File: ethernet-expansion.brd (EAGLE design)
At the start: 64.4 x 44.4 mm, 22 parts, among them Q1 25MHz, U1 ENC28J60-SO

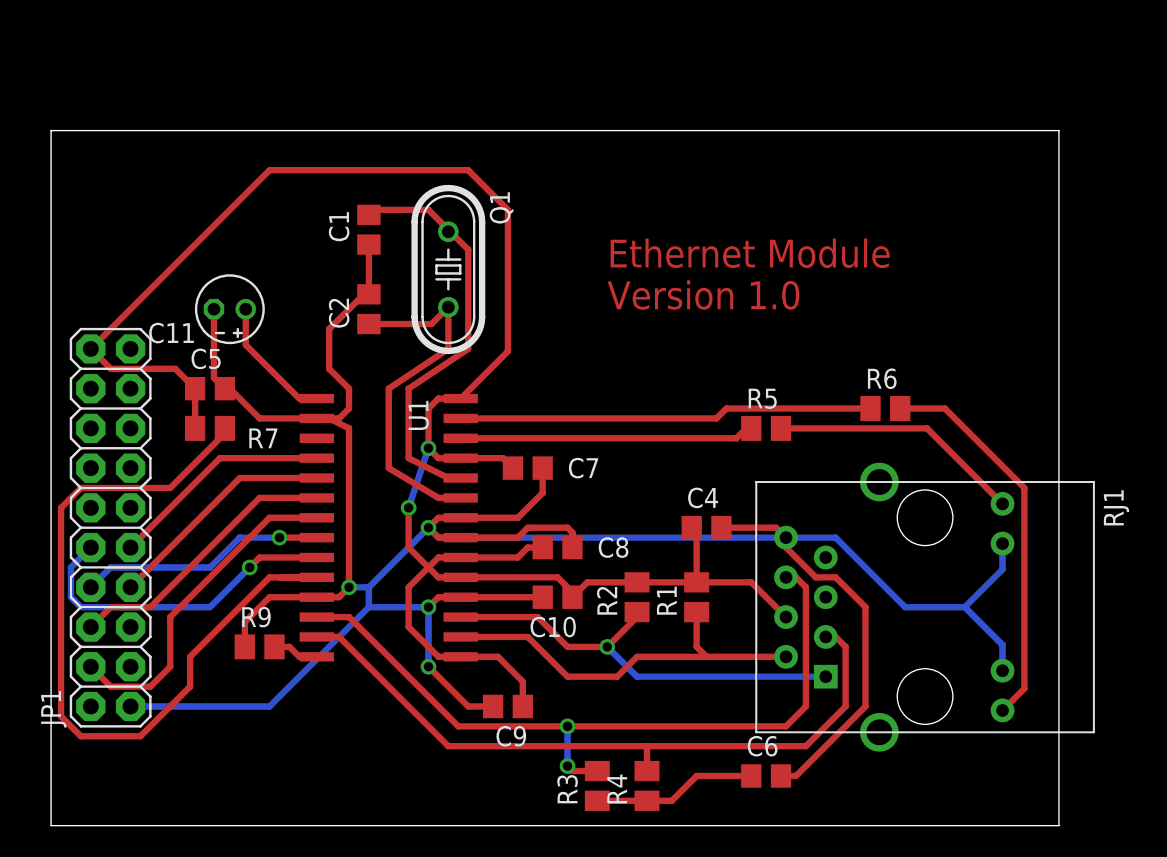
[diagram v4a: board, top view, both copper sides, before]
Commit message: Rotated oscillator to get a better Vdd trace
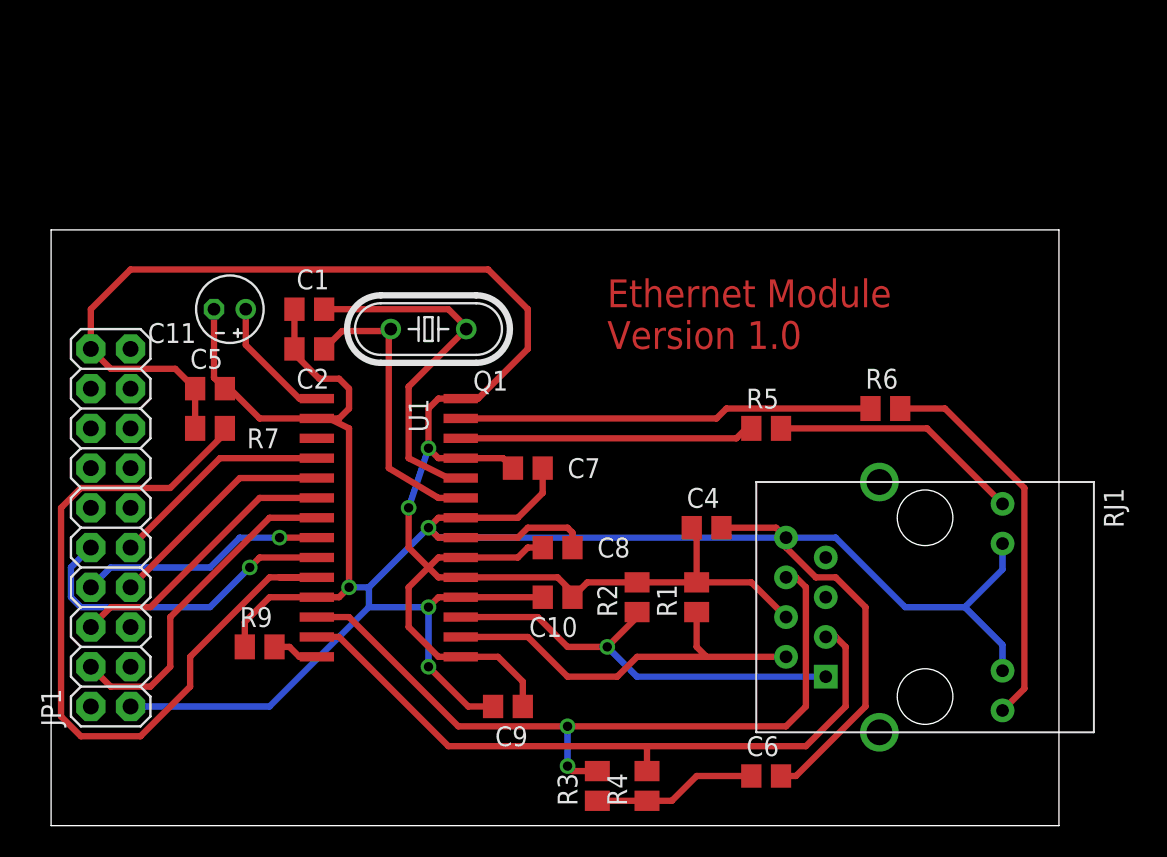
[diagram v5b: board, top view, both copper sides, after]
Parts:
- moved C1 6.35 mm to (16.5, 33.0), turned to 180 degrees
- moved C2 4.58 mm to (16.5, 30.5), turned to 180 degrees
- moved Q1 4.02 mm to (24.1, 31.8), turned to 180 degrees
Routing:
- net +3V3: track 126.5 -> 121.4 mm
- net N$12: track 23.0 -> 18.7 mm
- net GND: track 186.0 -> 182.2 mm
- net N$11: track 26.6 -> 23.1 mm
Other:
- board size 64.4 x 44.4 mm -> 64.4 x 38.1 mm
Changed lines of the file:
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@@
 <plain>
 <wire x1="0" y1="0" x2="64.44" y2="0" width="0" layer="20"/>
-<wire x1="64.44" y1="0" x2="64.44" y2="44.44" width="0" layer="20"/>
-<wire x1="64.44" y1="44.44" x2="0" y2="44.44" width="0" layer="20"/>
-<wire x1="0" y1="44.44" x2="0" y2="0" width="0" layer="20"/>
-<text x="35.56" y="33.02" size="1.778" layer="1">Ethernet Module
+<wire x1="64.44" y1="0" x2="64.44" y2="38.09" width="0" layer="20"/>
+<wire x1="64.44" y1="38.09" x2="0" y2="38.09" width="0" layer="20"/>
+<wire x1="0" y1="38.09" x2="0" y2="0" width="0" layer="20"/>
+<text x="35.56" y="30.48" size="1.778" layer="1">Ethernet Module
 Version 1.0</text>
 </plain>
@@
 <attribute name="NAME" x="44.45" y="4.445" size="1.27" layer="25"/>
 </element>
-<element name="C1" library="resistor" package="C0805" value="10pF" x="20.32" y="38.1" smashed="yes" rot="R270">
-<attribute name="NAME" x="17.78" y="39.37" size="1.27" layer="25" rot="R270"/>
-</element>
-<element name="C2" library="resistor" package="C0805" value="10pF" x="20.32" y="33.02" smashed="yes" rot="R90">
-<attribute name="NAME" x="19.05" y="31.75" size="1.27" layer="25" rot="R90"/>
+<element name="C1" library="resistor" package="C0805" value="10pF" x="16.51" y="33.02" smashed="yes" rot="R180">
+<attribute name="NAME" x="17.78" y="35.56" size="1.27" layer="25" rot="R180"/>
+</element>
+<element name="C2" library="resistor" package="C0805" value="10pF" x="16.51" y="30.48" smashed="yes" rot="R180">
+<attribute name="NAME" x="17.78" y="29.21" size="1.27" layer="25" rot="R180"/>
 </element>
 <element name="C5" library="resistor" package="C0805" value="0.1uF" x="10.16" y="27.94" smashed="yes">
@@
 </element>
 <element name="JP1" library="SparkFun-Connectors" package="2X10" value="" x="3.81" y="19.05" rot="R90"/>
-<element name="Q1" library="crystal" package="HC49/S" value="25MHz" x="25.4" y="35.56" rot="R270">
-<attribute name="OC_NEWARK" value="unknown" x="25.4" y="35.56" size="1.778" layer="27" rot="R270" display="off"/>
-<attribute name="MPN" value="" x="25.4" y="35.56" size="1.778" layer="27" rot="R270" display="off"/>
-<attribute name="MF" value="" x="25.4" y="35.56" size="1.778" layer="27" rot="R270" display="off"/>
-<attribute name="OC_FARNELL" value="1667008" x="25.4" y="35.56" size="1.778" layer="27" rot="R270" display="off"/>
+<element name="Q1" library="crystal" package="HC49/S" value="25MHz" x="24.13" y="31.75" rot="R180">
+<attribute name="OC_NEWARK" value="unknown" x="24.13" y="31.75" size="1.778" layer="27" rot="R180" display="off"/>
+<attribute name="MPN" value="" x="24.13" y="31.75" size="1.778" layer="27" rot="R180" display="off"/>
+<attribute name="MF" value="" x="24.13" y="31.75" size="1.778" layer="27" rot="R180" display="off"/>
+<attribute name="OC_FARNELL" value="1667008" x="24.13" y="31.75" size="1.778" layer="27" rot="R180" display="off"/>
 </element>
 <element name="R1" library="resistor" package="M0805" value="49.9" x="41.275" y="14.605" smashed="yes" rot="R90">
@@
 <contactref element="C7" pad="1"/>
 <contactref element="RJ1" pad="P4"/>
-<wire x1="2.54" y1="30.48" x2="13.97" y2="41.91" width="0.4064" layer="1"/>
-<wire x1="13.97" y1="41.91" x2="26.67" y2="41.91" width="0.4064" layer="1"/>
-<wire x1="26.67" y1="41.91" x2="29.21" y2="39.37" width="0.4064" layer="1"/>
-<wire x1="29.21" y1="39.37" x2="29.21" y2="30.325" width="0.4064" layer="1"/>
-<wire x1="29.21" y1="30.325" x2="26.19" y2="27.305" width="0.4064" layer="1"/>
 <wire x1="2.54" y1="30.48" x2="3.81" y2="29.21" width="0.4064" layer="1"/>
 <wire x1="3.81" y1="29.21" x2="7.94" y2="29.21" width="0.4064" layer="1"/>
@@
 <wire x1="37.465" y1="15.555" x2="34.285" y2="15.555" width="0.4064" layer="1"/>
 <wire x1="34.285" y1="15.555" x2="33.335" y2="14.605" width="0.4064" layer="1"/>
+<wire x1="5.08" y1="35.56" x2="27.94" y2="35.56" width="0.4064" layer="1"/>
+<wire x1="27.94" y1="35.56" x2="30.48" y2="33.02" width="0.4064" layer="1"/>
+<wire x1="30.48" y1="33.02" x2="30.48" y2="30.48" width="0.4064" layer="1"/>
+<wire x1="30.48" y1="30.48" x2="27.305" y2="27.305" width="0.4064" layer="1"/>
+<wire x1="27.305" y1="27.305" x2="26.19" y2="27.305" width="0.4064" layer="1"/>
+<wire x1="2.54" y1="30.48" x2="2.54" y2="33.02" width="0.4064" layer="1"/>
+<wire x1="2.54" y1="33.02" x2="5.08" y2="35.56" width="0.4064" layer="1"/>
 </signal>
 <signal name="GND">
@@
 <wire x1="10.414" y1="33.02" x2="10.414" y2="28.636" width="0.4064" layer="1"/>
 <wire x1="10.414" y1="28.636" x2="11.11" y2="27.94" width="0.4064" layer="1"/>
-<wire x1="20.32" y1="37.15" x2="20.32" y2="33.97" width="0.4064" layer="1"/>
-<wire x1="20.32" y1="33.97" x2="20" y2="33.97" width="0.4064" layer="1"/>
-<wire x1="20" y1="33.97" x2="17.78" y2="31.75" width="0.4064" layer="1"/>
-<wire x1="17.78" y1="31.75" x2="17.78" y2="29.21" width="0.4064" layer="1"/>
-<wire x1="17.78" y1="29.21" x2="19.05" y2="27.94" width="0.4064" layer="1"/>
+<wire x1="15.56" y1="33.02" x2="15.56" y2="30.48" width="0.4064" layer="1"/>
+<wire x1="17.78" y1="29.21" x2="18.415" y2="28.575" width="0" layer="19" extent="1-16"/>
+<wire x1="18.415" y1="28.575" x2="19.05" y2="27.94" width="0.4064" layer="1"/>
 <wire x1="19.05" y1="27.94" x2="19.05" y2="26.67" width="0.4064" layer="1"/>
 <wire x1="19.05" y1="26.67" x2="18.415" y2="26.035" width="0.4064" layer="1"/>
@@
 <wire x1="52.07" y1="13.97" x2="52.07" y2="7.62" width="0.4064" layer="1"/>
 <wire x1="52.07" y1="7.62" x2="47.625" y2="3.175" width="0.4064" layer="1"/>
+<wire x1="15.56" y1="30.48" x2="15.56" y2="30.16" width="0.4064" layer="1"/>
+<wire x1="15.56" y1="30.16" x2="17.145" y2="28.575" width="0.4064" layer="1"/>
+<wire x1="17.145" y1="28.575" x2="18.415" y2="28.575" width="0.4064" layer="1"/>
 </signal>
 <signal name="N$8">
@@
 <contactref element="U1" pad="24"/>
 <wire x1="25.4" y1="22.225" x2="26.19" y2="22.225" width="0.4064" layer="1"/>
-<wire x1="25.4" y1="37.973" x2="25.4" y2="38.1" width="0.4064" layer="1"/>
-<wire x1="25.4" y1="38.1" x2="24.13" y2="39.37" width="0.4064" layer="1"/>
-<wire x1="24.13" y1="39.37" x2="20.64" y2="39.37" width="0.4064" layer="1"/>
-<wire x1="20.64" y1="39.37" x2="20.32" y2="39.05" width="0.4064" layer="1"/>
-<wire x1="25.4" y1="37.973" x2="25.527" y2="37.973" width="0.4064" layer="1"/>
-<wire x1="25.527" y1="37.973" x2="26.67" y2="36.83" width="0.4064" layer="1"/>
-<wire x1="26.67" y1="36.83" x2="26.67" y2="30.48" width="0.4064" layer="1"/>
-<wire x1="26.67" y1="30.48" x2="22.86" y2="27.94" width="0.4064" layer="1"/>
-<wire x1="22.86" y1="27.94" x2="22.86" y2="23.495" width="0.4064" layer="1"/>
+<wire x1="22.86" y1="28.067" x2="22.86" y2="23.495" width="0.4064" layer="1"/>
 <wire x1="22.86" y1="23.495" x2="25.4" y2="22.225" width="0.4064" layer="1"/>
+<wire x1="22.86" y1="28.067" x2="26.543" y2="31.75" width="0.4064" layer="1"/>
+<wire x1="26.543" y1="31.75" x2="26.543" y2="31.877" width="0.4064" layer="1"/>
+<wire x1="26.543" y1="31.877" x2="25.4" y2="33.02" width="0.4064" layer="1"/>
+<wire x1="25.4" y1="33.02" x2="17.46" y2="33.02" width="0.4064" layer="1"/>
 </signal>
 <signal name="N$12">
@@
 <contactref element="C2" pad="1"/>
 <contactref element="U1" pad="23"/>
-<wire x1="25.4" y1="33.147" x2="25.4" y2="30.48" width="0.4064" layer="1"/>
-<wire x1="25.4" y1="30.48" x2="21.59" y2="27.94" width="0.4064" layer="1"/>
-<wire x1="21.59" y1="27.94" x2="21.59" y2="22.86" width="0.4064" layer="1"/>
+<wire x1="21.59" y1="31.623" x2="21.59" y2="22.86" width="0.4064" layer="1"/>
 <wire x1="21.59" y1="22.86" x2="24.765" y2="20.955" width="0.4064" layer="1"/>
 <wire x1="24.765" y1="20.955" x2="26.19" y2="20.955" width="0.4064" layer="1"/>
-<wire x1="20.32" y1="32.07" x2="24.323" y2="32.07" width="0.4064" layer="1"/>
-<wire x1="24.323" y1="32.07" x2="25.4" y2="33.147" width="0.4064" layer="1"/>
+<wire x1="21.59" y1="31.623" x2="21.717" y2="31.75" width="0.4064" layer="1"/>
+<wire x1="21.59" y1="31.623" x2="18.603" y2="31.623" width="0.4064" layer="1"/>
+<wire x1="18.603" y1="31.623" x2="17.46" y2="30.48" width="0.4064" layer="1"/>
 </signal>
 <signal name="ETH_INT0">

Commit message: Adding ground fill on top layer and trying out other placements
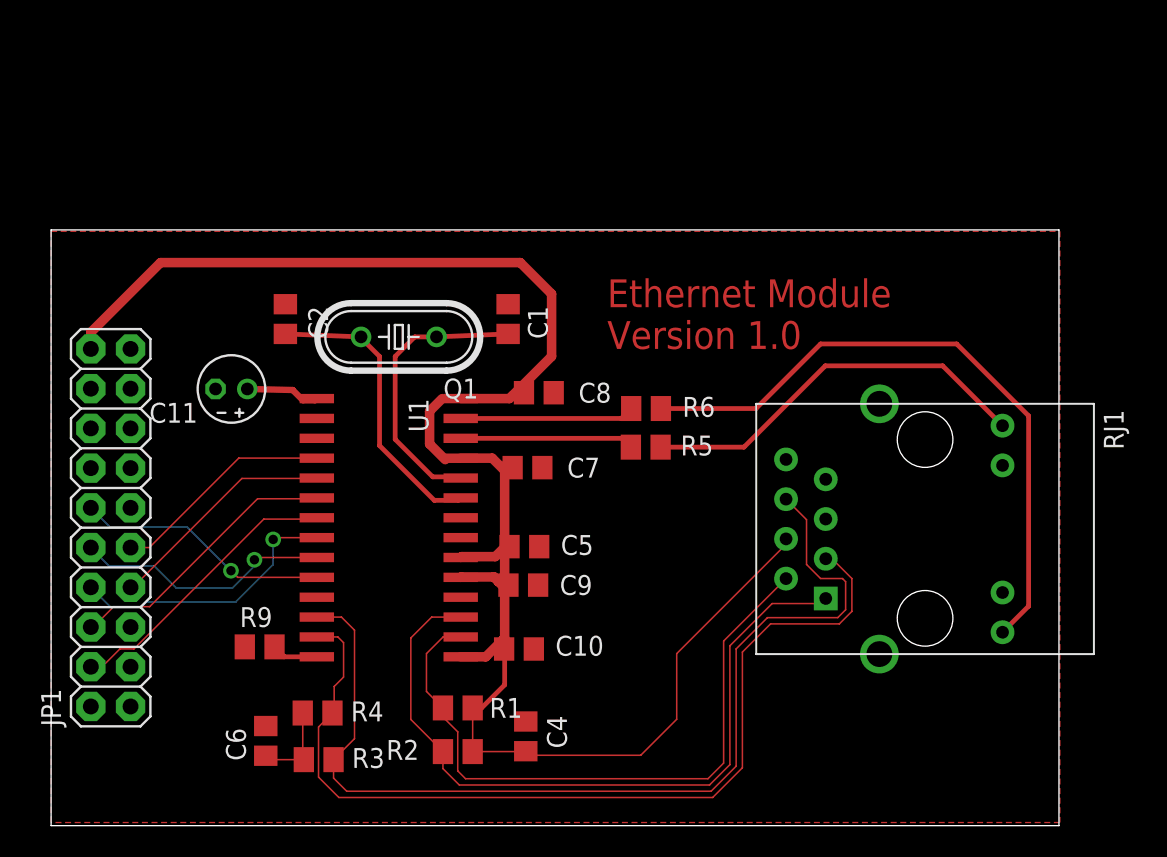
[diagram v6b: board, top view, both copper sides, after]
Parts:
- removed R7: 10K, resistor:M0805
- moved C6 32.1 mm to (13.7, 5.42), turned to 90 degrees
- moved C5 22.5 mm to (30.3, 17.8)
- moved R4 21.6 mm to (17.0, 7.20), turned to 0 degrees
- moved R3 17.9 mm to (17.1, 4.22), turned to 0 degrees
- moved C4 17.7 mm to (30.4, 5.71), turned to 90 degrees
- moved R1 16.8 mm to (26.0, 7.53), turned to 0 degrees
- moved R6 15.3 mm to (38.0, 26.7)
- moved R2 15.1 mm to (26.0, 4.74), turned to 0 degrees
- moved C1 12.7 mm to (29.2, 32.4), turned to 90 degrees
- moved C8 9.97 mm to (31.2, 27.7)
- moved C9 7.82 mm to (30.2, 15.4), turned to 0 degrees
- moved R5 7.79 mm to (38.0, 24.2)
- moved C11 5.10 mm to (11.5, 27.9)
- moved RJ1 5.00 mm to (55.9, 19.0)
- moved C10 4.13 mm to (29.9, 11.3), turned to 0 degrees
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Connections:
- removed net N$16: R7.1, U1.10
- new net ETH_RESET: JP1.12, U1.10
- net +3V3: no longer R7.2
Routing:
- net GND: track 182.2 -> 0.49 mm, vias 4 -> 0
- net N$16: track 50.7 -> 0.00 mm
- net N$1: track 27.9 -> 47.2 mm, vias 1 -> 0
- net N$10: track 24.8 -> 41.7 mm
- net N$2: track 25.5 -> 42.0 mm
- net ETH_RESET: track 0.00 -> 16.3 mm, vias 0 -> 1
- net N$4: track 48.4 -> 64.5 mm, vias 2 -> 0
- net GREEN: track 26.5 -> 11.2 mm
- net N$3: track 44.7 -> 59.3 mm
- net N$9: track 16.2 -> 25.6 mm
- net +3V3: track 121.4 -> 113.6 mm, vias 2 -> 0
- net YELLOW: track 18.8 -> 11.1 mm
- net N$8: track 10.5 -> 5.55 mm
- net N$11: track 23.1 -> 18.3 mm
- net ETH_CS: track 21.0 -> 16.6 mm
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- added copper zone on layer 1, net GND
